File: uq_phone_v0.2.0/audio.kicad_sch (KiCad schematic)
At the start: 31 parts, among them J1 PJ-605, U13 TS3A5018RSVR, U14 NAU88C22YG, U9 AZV5001RA4-7

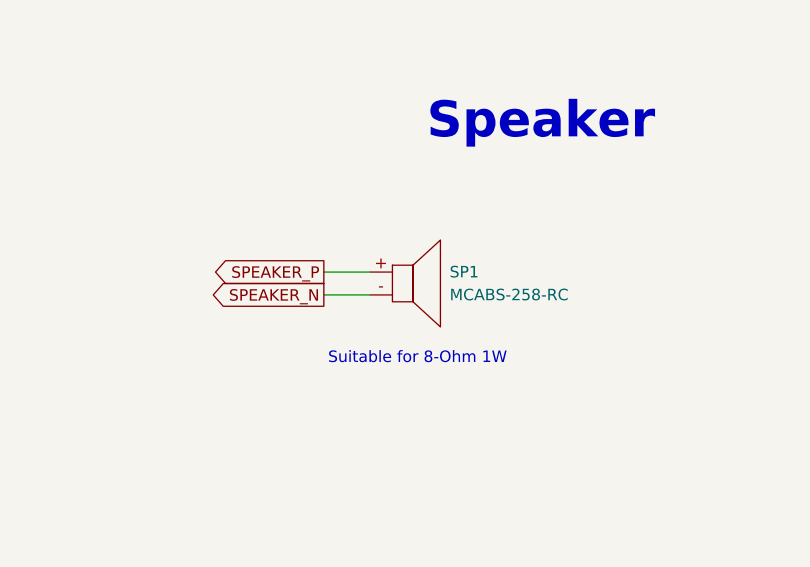
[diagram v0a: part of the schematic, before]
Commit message: Restructure, route and add flex pcb
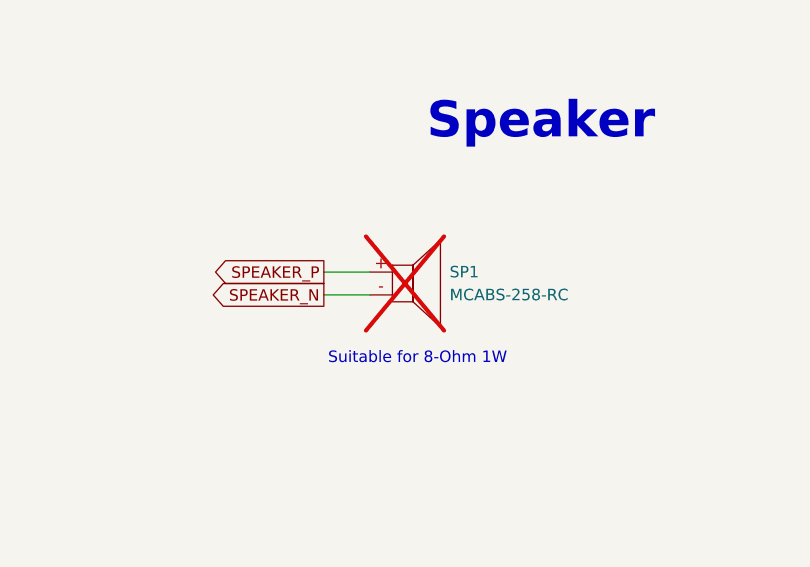
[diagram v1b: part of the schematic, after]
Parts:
- SP1: now not fitted
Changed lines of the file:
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@@
 		(in_bom yes)
 		(on_board yes)
-		(dnp no)
+		(dnp yes)
 		(fields_autoplaced yes)
 		(property "Reference" "SP1"

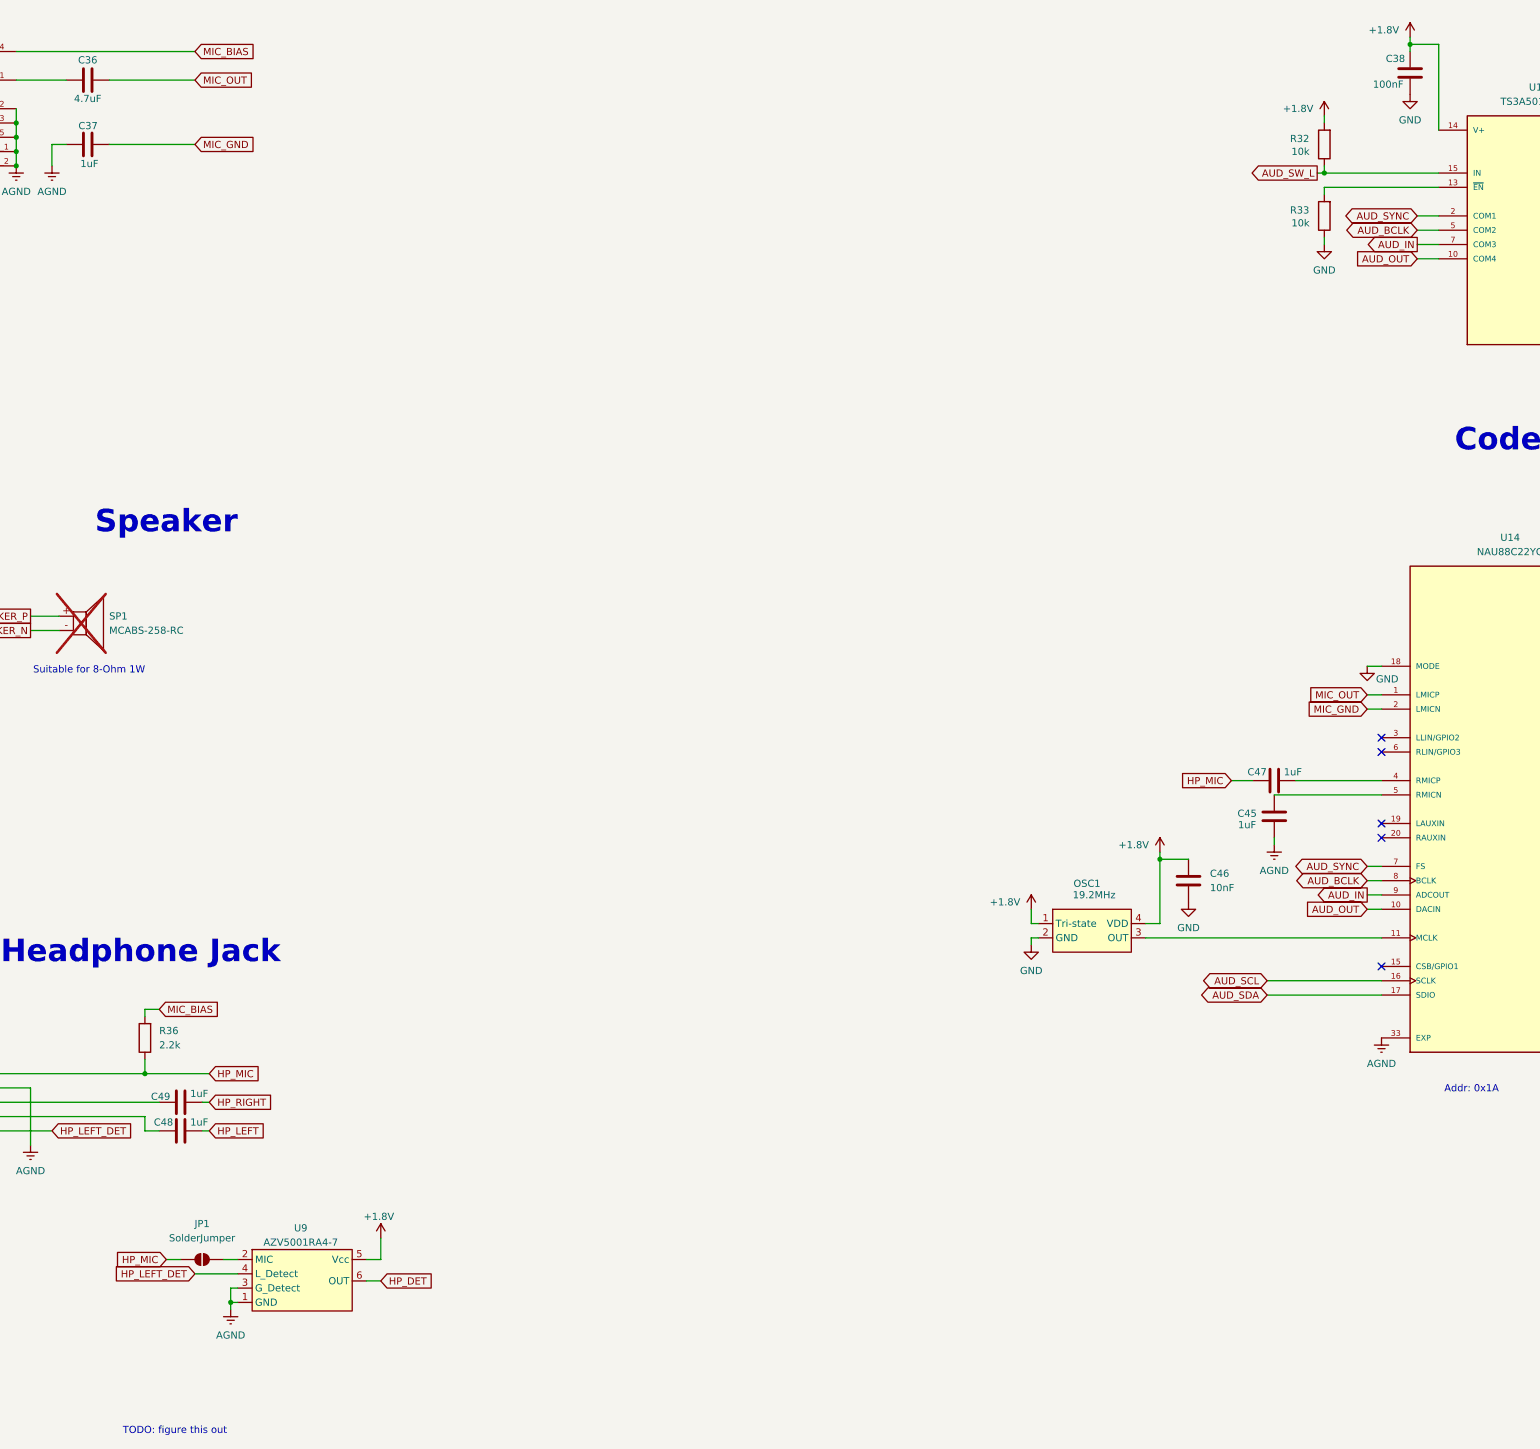
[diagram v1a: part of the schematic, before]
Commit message: New logic level shifters
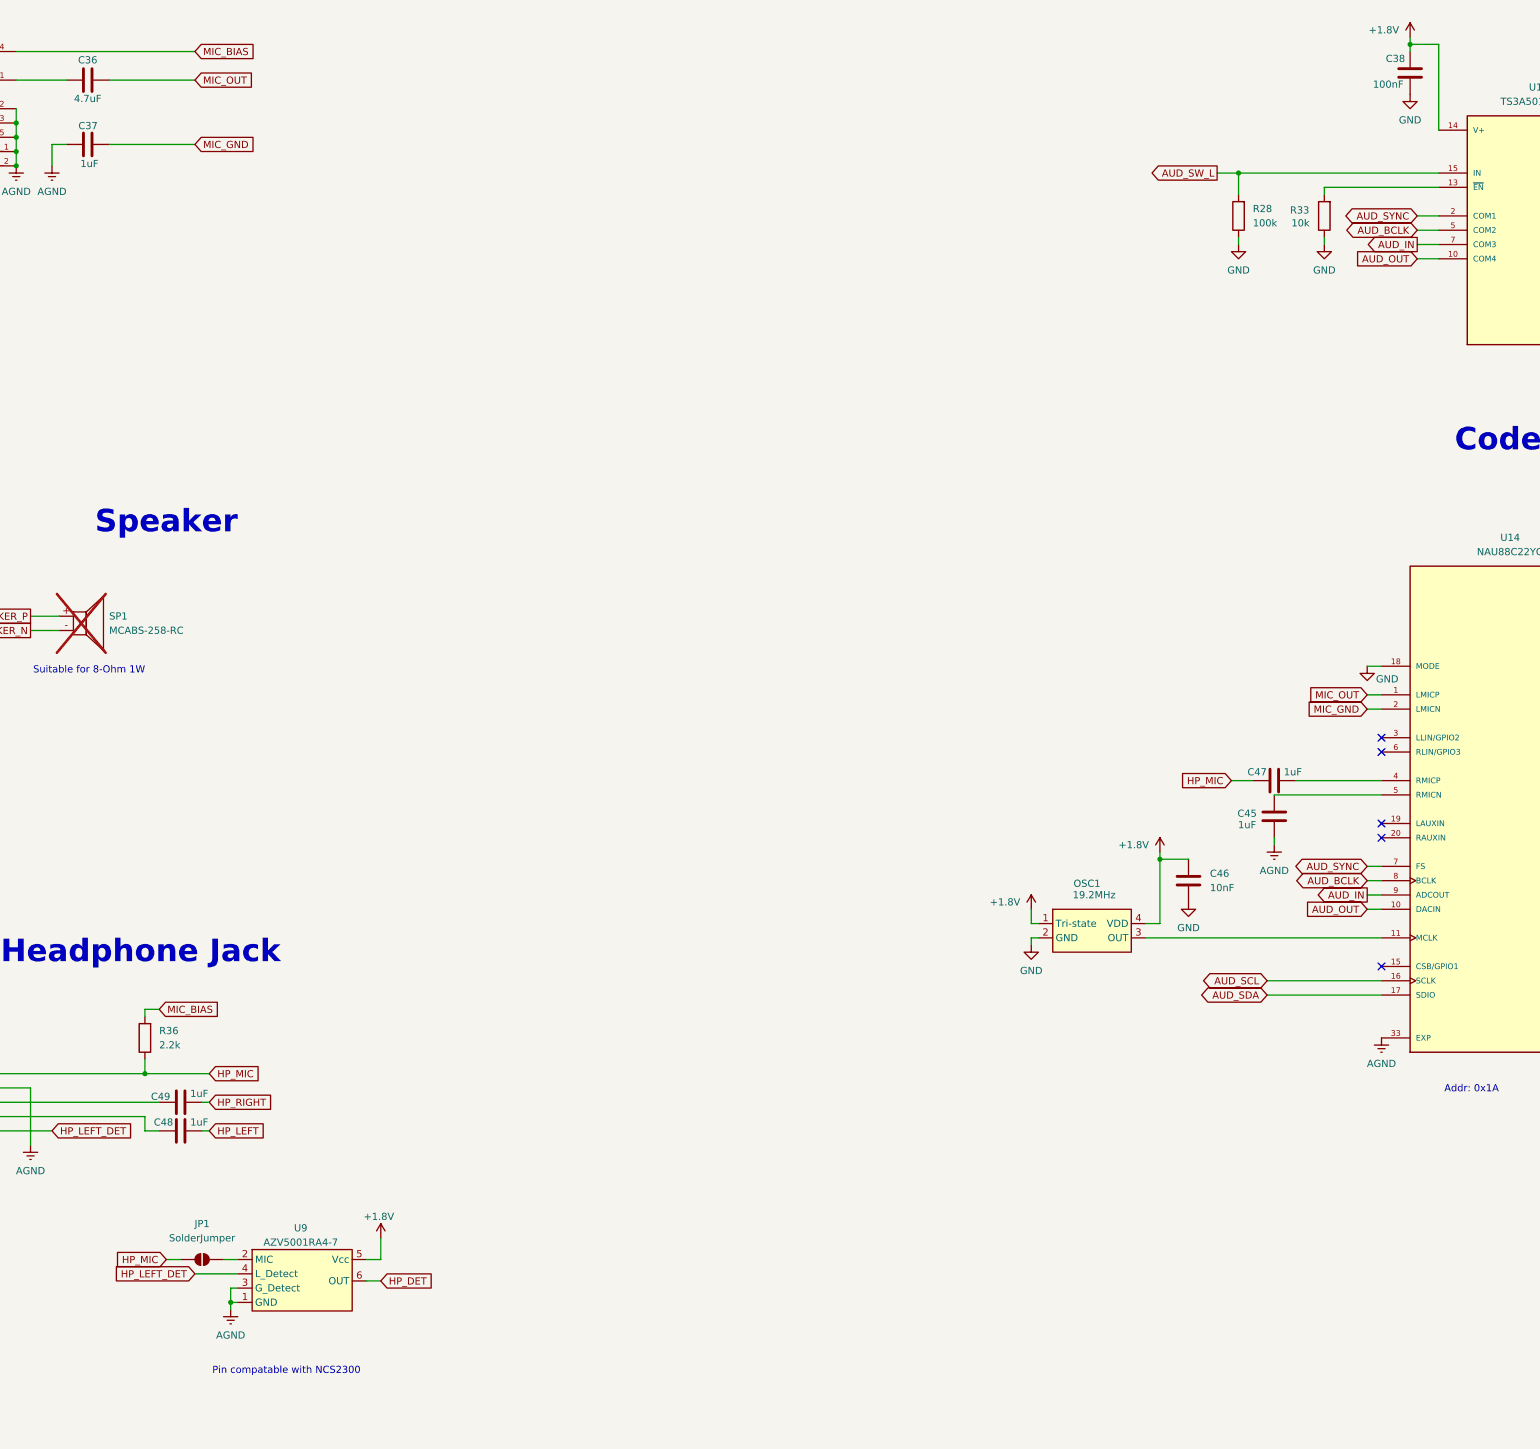
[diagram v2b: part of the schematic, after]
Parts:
- removed R32: 10k, Resistor_SMD:R_0201_0603Metric, symbol Resistors:Resistor_10k
- added R28: 100k, Resistor_SMD:R_0201_0603Metric, symbol Resistors:Resistor_100k
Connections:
- net AUD_SW_L: now also R28.2
- net GND: now also R28.1
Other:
- note added: "Pin compatable with NCS2300"
- note removed: "TODO: figure this out"
